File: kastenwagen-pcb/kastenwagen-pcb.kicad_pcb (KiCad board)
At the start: 2 copper layers, 112 parts, among them SW1 SW_Push, U1 Elite-C

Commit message: Reverse the stabilizers
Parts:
- MX417: footprint MX_Only:MXOnly-2.75U-NoLED -> MX_Only:MXOnly-2.75U-ReversedStabilizers-NoLED
- MX417.700: footprint MX_Only:MXOnly-7U-NoLED -> MX_Only:MXOnly-7U-ReversedStabilizers-NoLED
- MX437: footprint MX_Only:MXOnly-2.25U-NoLED -> MX_Only:MXOnly-2.25U-ReversedStabilizers-NoLED
- MX477.200: footprint MX_Only:MXOnly-2U-NoLED -> MX_Only:MXOnly-2U-ReversedStabilizers-NoLED
- MX487.200: footprint MX_Only:MXOnly-2U-ReversedStabilizers-NoLED -> MX_Only:MXOnly-2U-NoLED
- moved D477 1.63 mm to (341.1, 88.8)
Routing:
- net Col8: track 201.2 -> 194.8 mm
- net Net-(D477-Pad1): track 33.0 -> 39.1 mm
- net Row6: track 350.3 -> 352.5 mm
- net Net-(D477-Pad2): track 23.7 -> 25.3 mm
- net Net-(D437-Pad2): track 56.4 -> 57.9 mm
- net Net-(D375-Pad2): track 40.2 -> 41.2 mm
- net Col7: track 163.2 -> 164.0 mm

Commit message: drawing edge cuts
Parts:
- D1, D2, D3: footprint LED_THT:LED_D3.0mm -> LED_SMD:LED_1206_3216Metric_Pad1.42x1.75mm_HandSolder
- turned D1 to 180 degrees
- turned D2 to 180 degrees
- turned D3 to 180 degrees
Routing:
- net LED2: track 5.29 -> 9.32 mm
- net LED1: track 17.0 -> 13.1 mm, vias 0 -> 1
- net LED3: track 8.63 -> 12.0 mm
- net LED3R: track 23.8 -> 21.3 mm
- net LED2R: track 13.6 -> 11.1 mm
- net LED1R: track 22.7 -> 20.6 mm
- net Rotary0A: track 269.5 -> 270.8 mm
- net Rotary0B: track 267.2 -> 268.5 mm
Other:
- board outline added: 350.5 x 83.5 mm
- board text added: ">"

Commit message: Ground planes
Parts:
- removed SW1: SW_Push, Keebio-Parts:SW_Tactile_SPST_Angled_MJTP1117
- R1, R2, R3: footprint Keebio-Parts:Resistor-Hybrid-Back -> Keebio-Parts:R_0805; moved to B.Cu
- moved R3 9.98 mm to (296.9, 32.9), turned to 180 degrees
- turned R1 to 180 degrees
- turned R2 to 180 degrees
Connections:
- U1 pad 22: RESET -> Net-(U1-Pad22)
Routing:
- net GND: track 378.2 -> 2201.3 mm, vias 1 -> 185
- net RESET: track 15.3 -> 0.00 mm
- net LED3R: track 21.3 -> 15.9 mm, vias 0 -> 1
- net LED1R: track 20.6 -> 23.6 mm, vias 0 -> 1
- net LED2R: track 11.1 -> 14.1 mm, vias 0 -> 1
- net Net-(U1-Pad22): track 0.00 -> 1.78 mm
- net Net-(D170-Pad2): track 35.5 -> 37.0 mm
- net Rotary0B: track 268.5 -> 267.1 mm
- net Rotary0A: track 270.8 -> 269.9 mm
- net LED2: track 9.32 -> 10.1 mm
- net Row5: track 295.4 -> 296.0 mm
- added copper zone on B.Cu, net GND
- added copper zone on F.Cu, net GND

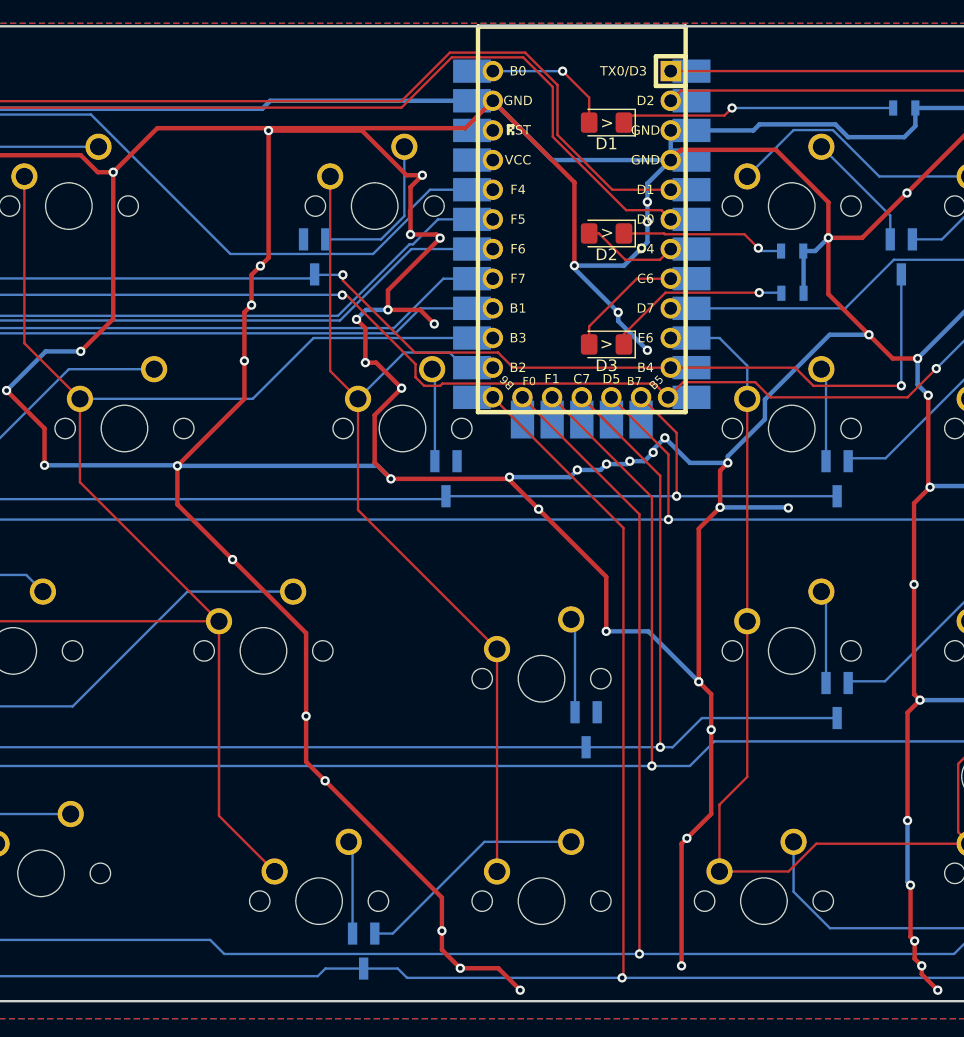
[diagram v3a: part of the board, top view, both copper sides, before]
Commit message: Plate edits and LED positioning
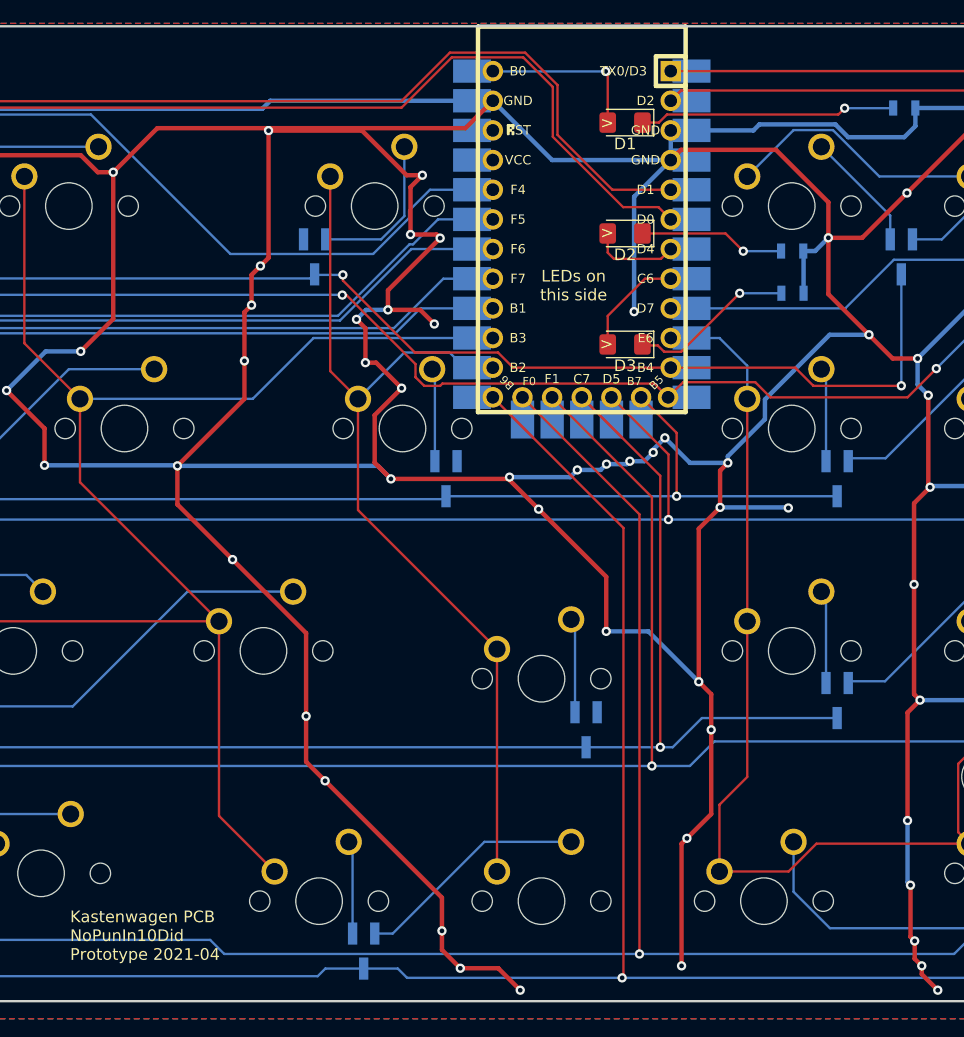
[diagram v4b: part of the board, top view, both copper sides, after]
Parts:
- moved D1 1.59 mm to (282.6, 18.2)
- moved D2 1.59 mm to (282.6, 27.7)
- moved D3 1.59 mm to (282.6, 37.2)
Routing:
- net GND: track 2201.3 -> 2173.8 mm, vias 185 -> 180
- net LED1: track 13.1 -> 15.9 mm
- net LED3R: track 15.9 -> 14.2 mm
- net LED1R: track 23.6 -> 22.0 mm
- net LED2R: track 14.1 -> 12.5 mm
- net LED3: track 12.0 -> 10.9 mm
- net LED2: track 10.1 -> 9.39 mm
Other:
- board text added: "Kastenwagen PCB NoPunIn10Did Prototype 2021-04"
- board text added: "LEDs on this side"
- board text added: "Solder Elite C to THIS side of the PCB"

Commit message: Kastenwagen 1840 PCB Gerbers
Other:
- board text added: "Build Notes: Diodes, Elite C, & Resistors all surface-mount to this side of the PCB (bottom). LEDs should be surface-mounted to the top side. Install LEDs before adding switches."

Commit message: Further gerber updates
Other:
- board text added: "Kastenwagen PCB NoPunIn10Did Prototype 2021-06"
- board text removed: "Kastenwagen PCB NoPunIn10Did Prototype 2021-04"
